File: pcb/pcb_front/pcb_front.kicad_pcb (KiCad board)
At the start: 2 copper layers, 30 x 27 mm, 24 parts, among them J1 MicroLab, J2 LED_BREAKOUT, J3 GAS_BREAKOUT, U1 TBD62783A

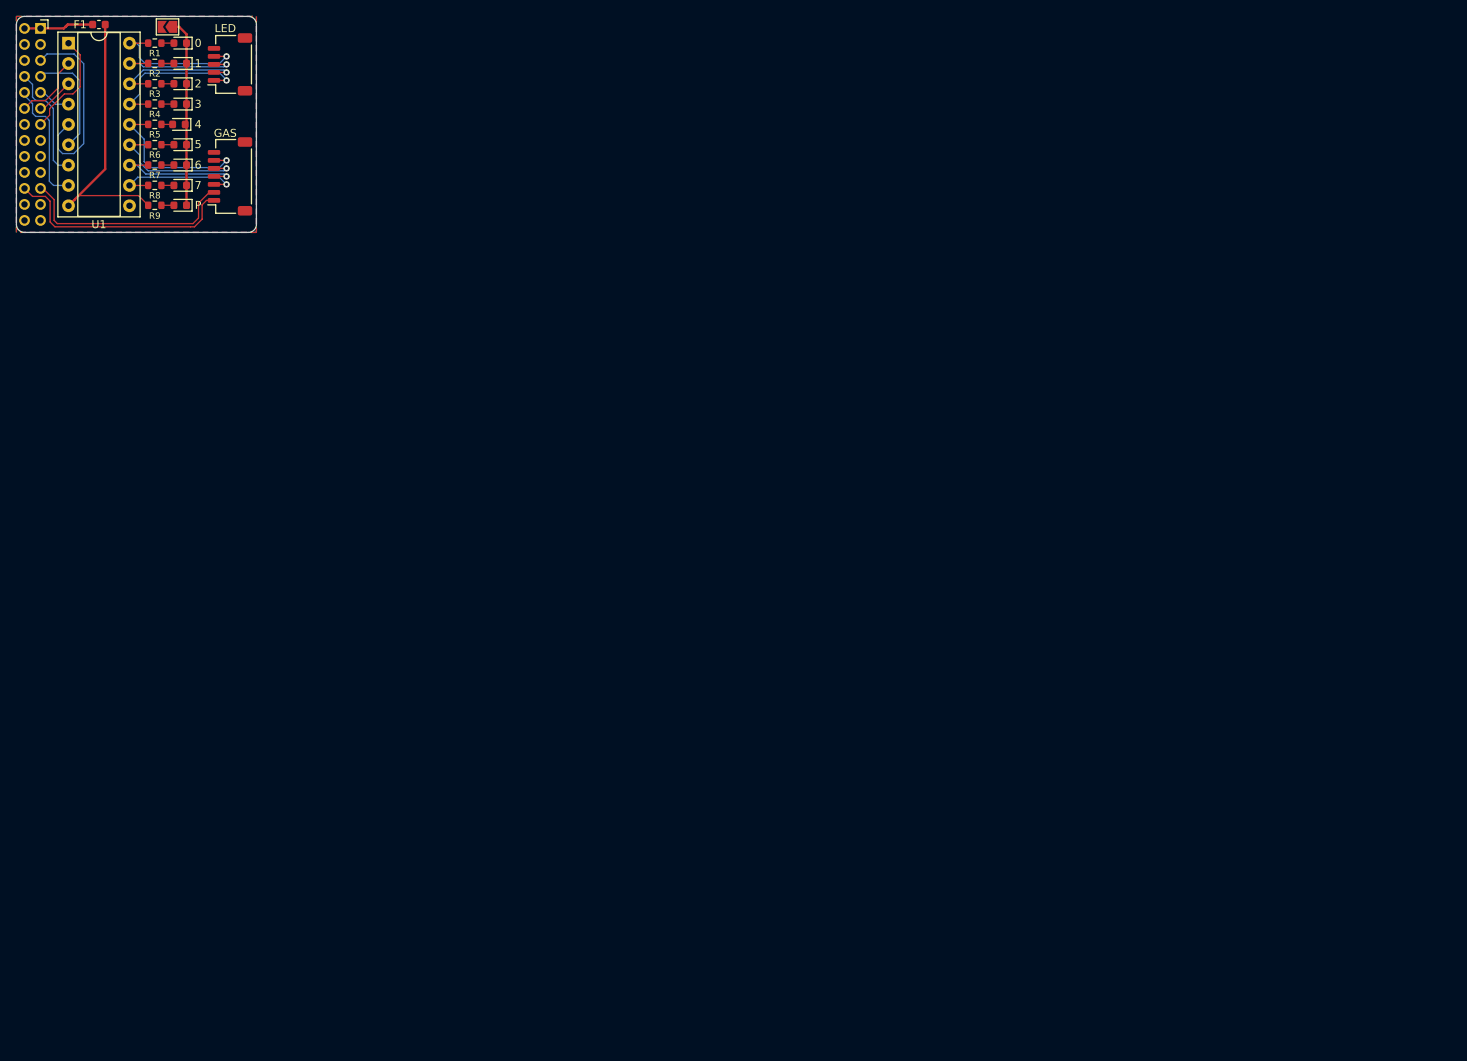
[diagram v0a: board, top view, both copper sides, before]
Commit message: curved gnd plane on corners
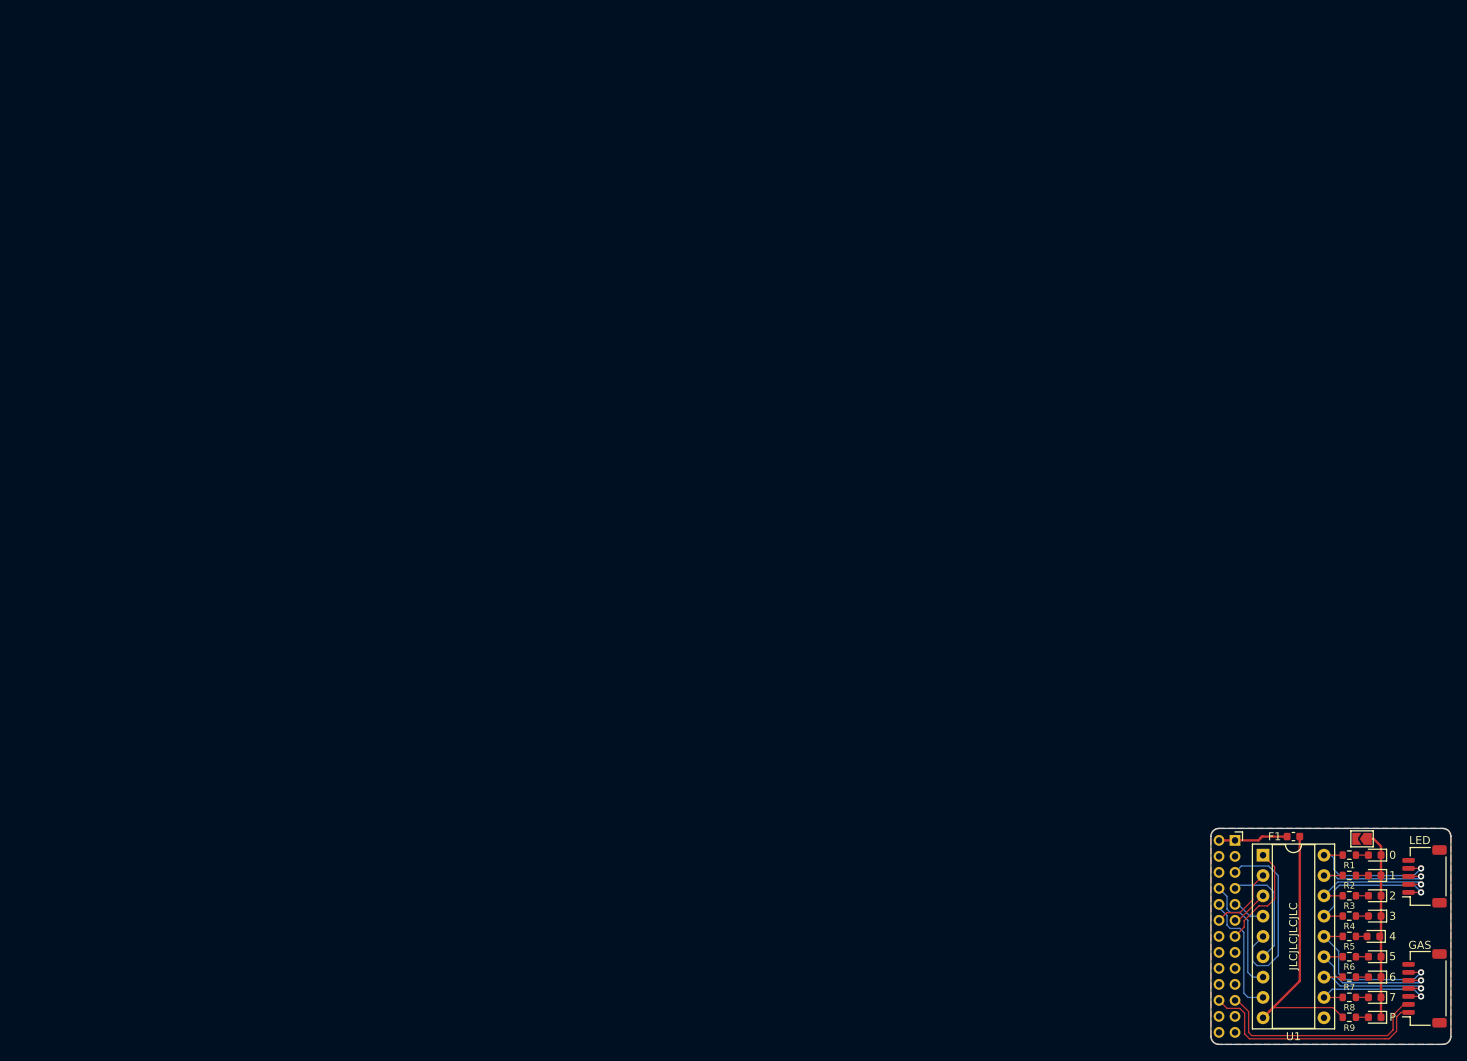
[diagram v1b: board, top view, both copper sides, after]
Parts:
- moved D1 180.5 mm to (159.5, 91.3)
- moved D2 180.5 mm to (159.5, 93.9)
- moved D3 180.5 mm to (159.5, 96.4)
- moved D4 180.5 mm to (159.5, 99.0)
- moved D5 180.5 mm to (159.3, 101.5)
- moved D6 180.5 mm to (159.5, 104.0)
- moved D7 180.5 mm to (159.5, 106.6)
- moved D8 180.5 mm to (159.5, 109.1)
- moved D9 180.5 mm to (159.5, 111.6)
- moved F1 180.5 mm to (149.3, 89.0)
- moved J1 180.5 mm to (142.0, 89.5)
- moved J2 180.5 mm to (165.7, 94.0)
- moved J3 180.5 mm to (165.7, 108.0)
- moved JP1 180.5 mm to (157.9, 89.3)
- moved R1 180.5 mm to (156.3, 91.3)
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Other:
- board text added: "JLCJLCJLCJLC"

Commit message: front pcb rev 2
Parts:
- removed D2: IO1, LED_SMD:LED_0603_1608Metric
- removed D3: IO2, LED_SMD:LED_0603_1608Metric
- removed D4: IO3, LED_SMD:LED_0603_1608Metric
- removed D5: IO4, LED_SMD:LED_0603_1608Metric
- removed D6: IO5, LED_SMD:LED_0603_1608Metric
- removed D7: IO6, LED_SMD:LED_0603_1608Metric
- removed D8: IO7, LED_SMD:LED_0603_1608Metric
- removed D9: PWR, LED_SMD:LED_0603_1608Metric
- removed F1: Polyfuse_Small, Fuse:Fuse_0603_1608Metric
- removed JP1: SolderJumper_2_Open, Jumper:SolderJumper-2_P1.3mm_Open_TrianglePad1.0x1.5mm
- removed R2, R3, R4, R5, R6, R7, R8, R9: 2K, Resistor_SMD:R_0603_1608Metric
- removed U1: TBD62783A, Package_DIP:DIP-18_W7.62mm_Socket
- added H1: M2, MountingHole:MountingHole_2.2mm_M2_DIN965_Pad, F.Cu at (5.75, -0.25)
- added H2: M2, MountingHole:MountingHole_2.2mm_M2_DIN965_Pad, F.Cu at (5.75, 24.8)
- added H3: M2, MountingHole:MountingHole_2.2mm_M2_DIN965_Pad, F.Cu at (25.5, 24.8)
- D1: value IO0 -> LED; footprint LED_SMD:LED_0603_1608Metric -> LED_SMD:LED_0402_1005Metric_Pad0.77x0.64mm_HandSolder
- J1: footprint Connector_PinSocket_2.00mm:PinSocket_2x13_P2.00mm_Horizontal -> Connector_PinHeader_2.00mm:PinHeader_2x13_P2.00mm_Vertical; moved to B.Cu
- J2: value LED_BREAKOUT -> Gas Breakout; footprint Connector_JST:JST_SH_SM05B-SRSS-TB_1x05-1MP_P1.00mm_Horizontal -> Connector_JST:JST_SH_BM08B-SRSS-TB_1x08-1MP_P1.00mm_Vertical
- J3: value GAS_BREAKOUT -> LED Breakout; footprint Connector_JST:JST_SH_SM07B-SRSS-TB_1x07-1MP_P1.00mm_Horizontal -> Connector_JST:JST_SH_BM05B-SRSS-TB_1x05-1MP_P1.00mm_Vertical
- R1: footprint Resistor_SMD:R_0603_1608Metric -> Resistor_SMD:R_0402_1005Metric_Pad0.72x0.64mm_HandSolder
- moved J2 168.3 mm to (10.2, 29.5), turned to 180 degrees
- moved J1 166.2 mm to (2.00, 0.00), turned to 180 degrees
- moved J3 163.2 mm to (22.6, 29.5), turned to 180 degrees
- moved D1 154.6 mm to (17.2, 30.9), turned to 90 degrees
- moved R1 152.6 mm to (17.2, 28.6), turned to 90 degrees
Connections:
- D1 pad 1: Net-(D1-Pad1) -> GND
- J1 pad 1: Net-(J1-Pad1) -> +5V
- J1 pad 2: Net-(J1-Pad1) -> +5V
- J2 pad 1: /V_PUMP_LYO -> +5V
- J2 pad 2: /V_PUMP_CARB -> /IO4
- J2 pad 3: /V_LED_BACT -> /IO5
- J2 pad 4: /V_LED_CAM -> /IO6
- J2 pad 5: GND -> /IO3
- J2 pad MP: (no net) -> GND
- J3 pad 1: /SDA -> +5V
- J3 pad 2: /SCL -> /IO2
- J3 pad 3: /V_FAN -> /IO1
- J3 pad 4: /V_O2 -> /IO0
- J3 pad 5: /V_CO2 -> GND
- J3 pad MP: (no net) -> GND
- R1 pad 2: /V_LED_CAM -> +5V
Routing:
- net /IO2: track 4.79 -> 35.5 mm, vias 0 -> 1
- net /IO1: track 8.87 -> 36.4 mm, vias 0 -> 1
- net Net-(D1-Pad1): track 23.4 -> 0.00 mm
- net /IO3: track 4.11 -> 25.8 mm
- net /V_CH4: track 20.3 -> 0.00 mm, vias 1 -> 0
- net /IO0: track 13.4 -> 32.7 mm, vias 0 -> 1
- net /V_PUMP_LYO: track 19.2 -> 0.00 mm, vias 1 -> 0
- net /V_LED_CAM: track 18.3 -> 0.00 mm, vias 1 -> 0
- net /V_CO2: track 18.0 -> 0.00 mm, vias 1 -> 0
- net +5V: track 34.4 -> 52.2 mm
- net /V_PUMP_CARB: track 16.9 -> 0.00 mm, vias 1 -> 0
- net /V_FAN: track 16.8 -> 0.00 mm, vias 1 -> 0
- net /V_O2: track 16.6 -> 0.00 mm, vias 1 -> 0
- net /V_LED_BACT: track 16.3 -> 0.00 mm, vias 1 -> 0
- net /IO7: track 15.7 -> 0.00 mm
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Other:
- board size 30 x 27 mm -> 29.8 x 34.9 mm
- board text added: "JLCJLCJLC"
- board text added: "LED"
- board text added: "MicroLab"
- board text added: "SAS SpaceLab 2023 Emilio Orcullo"
- board text added: "Sensors"
- board text removed: "JLCJLCJLCJLC"

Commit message: fin
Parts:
- J2: value Gas Breakout -> Sensors; footprint Connector_JST:JST_SH_BM08B-SRSS-TB_1x08-1MP_P1.00mm_Vertical -> Connector_JST:JST_SH_BM04B-SRSS-TB_1x04-1MP_P1.00mm_Vertical
- J3: value LED Breakout -> LED
- moved D1 37.0 mm to (-0.27, -1.65), turned to 0 degrees
- moved R1 33.8 mm to (2.30, -1.65), turned to 0 degrees
- moved H2 5.86 mm to (5.75, 30.6)
- moved H3 5.86 mm to (25.5, 30.6)
- moved J3 3.41 mm to (19.2, 30.1)
- moved J2 1.45 mm to (11.5, 30.1)
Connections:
- J2 pad 2: /IO4 -> /SDA
- J2 pad 3: /IO5 -> /SCL
- J2 pad 4: /IO6 -> GND
- J3 pad 2: /IO2 -> /IO3
- J3 pad 3: /IO1 -> /IO2
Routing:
- net /IO1: track 36.4 -> 0.00 mm, vias 1 -> 0
- net /IO4: track 32.7 -> 0.00 mm
- net /IO6: track 28.8 -> 0.00 mm
- net /IO5: track 27.5 -> 0.00 mm
- net /IO3: track 25.8 -> 37.8 mm
- net +5V: track 52.2 -> 59.2 mm
- net /IO2: track 35.5 -> 32.9 mm, vias 1 -> 0
- net /IO0: track 32.7 -> 30.4 mm, vias 1 -> 0
- net /SDA: track 18.1 -> 19.9 mm
- net /SCL: track 14.5 -> 16.0 mm
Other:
- outline, holes or cut-outs redrawn
- board text added: "JLCJLCJLCJLC"
- board text added: "SAS SpaceLab 2023"
- board text removed: "JLCJLCJLC"
- board text removed: "SAS SpaceLab 2023 Emilio Orcullo"

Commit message: production ver. of PCB
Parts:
- added D2: D_Small, Diode_SMD:D_SOD-323, F.Cu at (43.0, 22.0)
- added D3: D_Small, Diode_SMD:D_SOD-323, F.Cu at (43.0, 19.1)
- added D4: D_Small, Diode_SMD:D_SOD-323, F.Cu at (47.2, 19.1)
- added H4: M2, MountingHole:MountingHole_2.2mm_M2_DIN965_Pad, F.Cu at (28.0, 32.5)
- added J4: Pump 2, Connector_JST:JST_SH_BM02B-SRSS-TB_1x02-1MP_P1.00mm_Vertical, F.Cu at (44.3, 14.4)
- added J5: LED, Connector_JST:JST_SH_BM02B-SRSS-TB_1x02-1MP_P1.00mm_Vertical, F.Cu at (58.0, 14.4)
- added R2: 10K, Resistor_SMD:R_0402_1005Metric, F.Cu at (46.6, 21.5)
- added R3: 10K, Resistor_SMD:R_0402_1005Metric, F.Cu at (50.8, 18.6)
- added R4: 10K, Resistor_SMD:R_0402_1005Metric, F.Cu at (49.5, 21.5)
- J1: moved to F.Cu
- J3: value LED -> Pump 1; footprint Connector_JST:JST_SH_BM05B-SRSS-TB_1x05-1MP_P1.00mm_Vertical -> Connector_JST:JST_SH_BM02B-SRSS-TB_1x02-1MP_P1.00mm_Vertical
- moved D1 58.8 mm to (58.0, 6.50)
- moved J2 45.8 mm to (48.0, 2.38), turned to 0 degrees
- moved R1 44.5 mm to (46.0, 6.50)
- moved H2 37.9 mm to (28.0, 0.00)
- moved J3 35.6 mm to (51.1, 14.4), turned to 0 degrees
- moved J1 28.6 mm to (-3.77, 28.0)
- moved H3 25.6 mm to (0.00, 32.5)
- moved H1 5.76 mm to (0.00, 0.00)
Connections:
- J3 pad 2: /IO3 -> Net-(D2-Pad2)
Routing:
- net +5V: track 59.2 -> 0.00 mm
- net /IO3: track 37.8 -> 0.00 mm
- net /IO2: track 32.9 -> 0.00 mm
- net /IO0: track 30.4 -> 0.00 mm
- net /SDA: track 19.9 -> 0.00 mm
- net /SCL: track 16.0 -> 0.00 mm
- net Net-(D1-Pad2): track 1.40 -> 0.00 mm
- removed copper zone on B.Cu, net GND
- removed copper zone on F.Cu, net GND
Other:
- board size 29.8 x 34.9 mm -> 42.1 x 37.9 mm
- board text removed: "JLCJLCJLCJLC"
- board text removed: "LED"
- board text removed: "MicroLab"
- board text removed: "SAS SpaceLab 2023"
- board text removed: "Sensors"
